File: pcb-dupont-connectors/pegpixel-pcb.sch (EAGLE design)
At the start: 6 parts

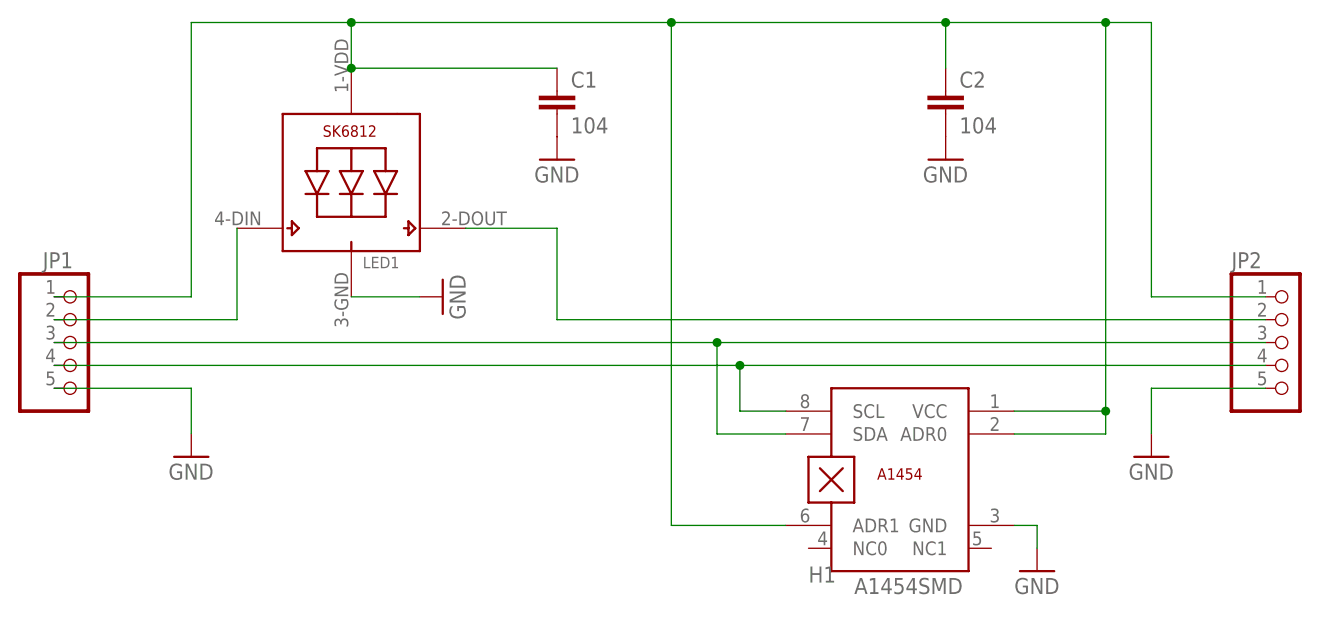
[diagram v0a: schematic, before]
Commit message: Remove second capacitor
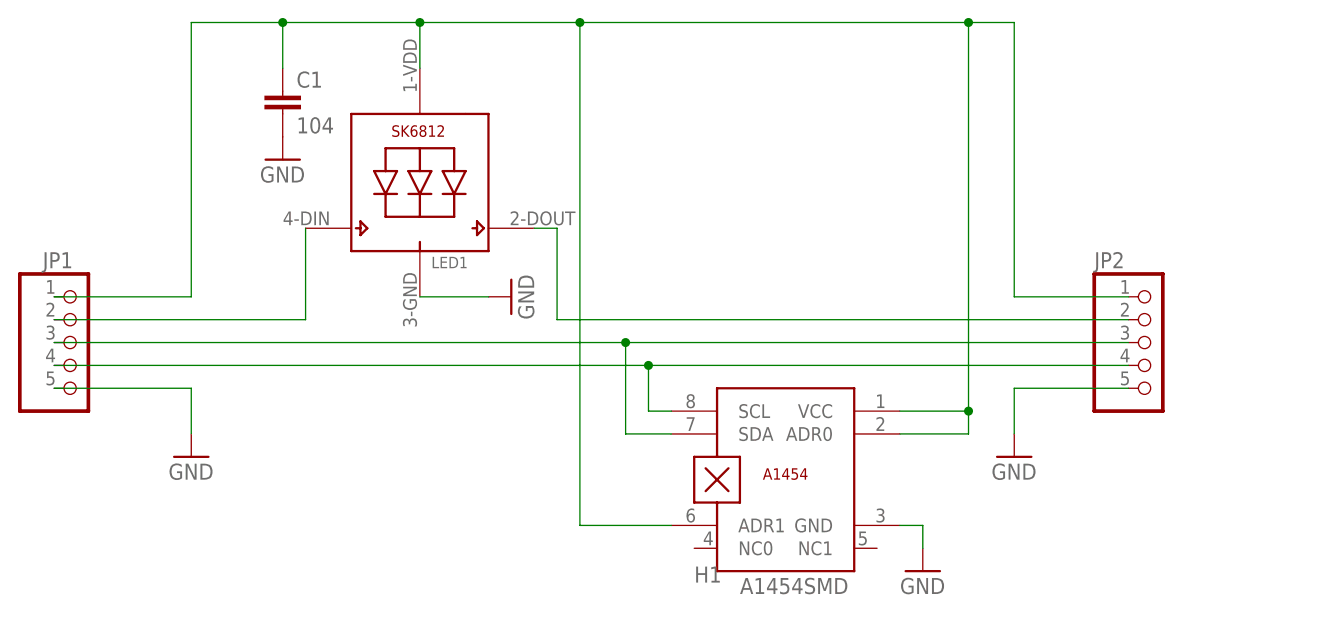
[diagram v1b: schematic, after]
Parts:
- removed C2: 104, rcl:C-EUC0805
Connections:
- net GND: no longer C2.2
- net VCC: no longer C2.1
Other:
- moved on the sheet: C1, H1, JP2, LED1

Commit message: pcb-design: add missing GRND-via
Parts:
- renumbered C1 to 104
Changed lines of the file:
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@@
 <parts>
 <part name="LED1" library="SK6812" deviceset="SK6812" device="_5050"/>
-<part name="C1" library="rcl" library_urn="urn:adsk.eagle:library:334" deviceset="C-EU" device="C0805" package3d_urn="urn:adsk.eagle:package:23617/2" value="104"/>
+<part name="104" library="rcl" library_urn="urn:adsk.eagle:library:334" deviceset="C-EU" device="C0805" package3d_urn="urn:adsk.eagle:package:23617/2" value="104"/>
 <part name="H1" library="a1454" deviceset="A1454" device="SMD" package3d_urn="urn:adsk.eagle:package:20813/2"/>
 <part name="GND1" library="supply1" library_urn="urn:adsk.eagle:library:371" deviceset="GND" device=""/>
@@
 <attribute name="VALUE" x="44.45" y="54.61" size="1.27" layer="96"/>
 </instance>
-<instance part="C1" gate="G$1" x="27.94" y="76.2" smashed="yes">
+<instance part="104" gate="G$1" x="27.94" y="76.2" smashed="yes">
 <attribute name="NAME" x="29.464" y="76.581" size="1.778" layer="95"/>
 <attribute name="VALUE" x="29.464" y="71.501" size="1.778" layer="96"/>
@@
 <junction x="104.14" y="83.82"/>
 <junction x="27.94" y="83.82"/>
-<pinref part="C1" gate="G$1" pin="1"/>
+<pinref part="104" gate="G$1" pin="1"/>
 <wire x1="27.94" y1="78.74" x2="27.94" y2="83.82" width="0.1524" layer="91"/>
 </segment>
@@
 <net name="GND" class="0">
 <segment>
-<pinref part="C1" gate="G$1" pin="2"/>
+<pinref part="104" gate="G$1" pin="2"/>
 <pinref part="GND3" gate="1" pin="GND"/>
 </segment>

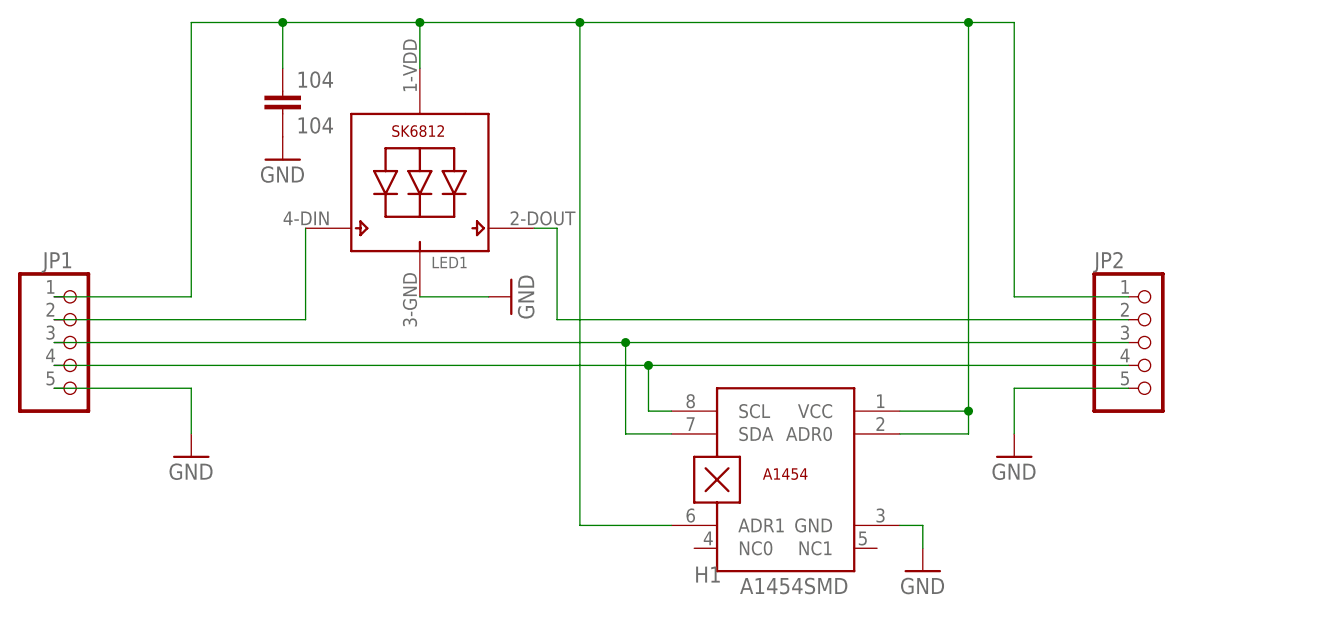
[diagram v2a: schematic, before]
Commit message: mirror and turn input pin header to place it on top layer
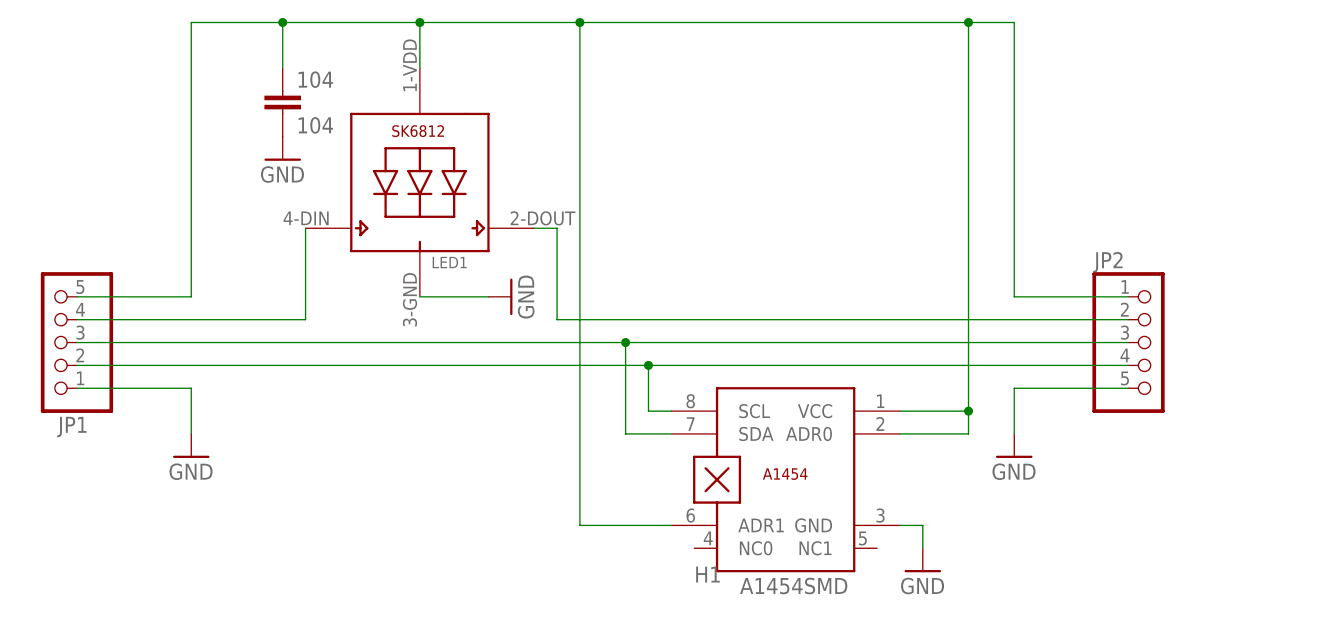
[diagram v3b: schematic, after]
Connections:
- net DIN: now also JP1.4; no longer JP1.2
- net GND: now also JP1.1; no longer JP1.5
- net SCL: now also JP1.2; no longer JP1.4
- net VCC: now also JP1.5; no longer JP1.1
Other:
- moved on the sheet: JP1
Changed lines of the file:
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@@
 <setting verticaltext="up"/>
 </settings>
-<grid distance="0.1" unitdist="inch" unit="inch" style="lines" multiple="1" display="yes" altdistance="0.01" altunitdist="inch" altunit="inch"/>
+<grid distance="0.1" unitdist="inch" unit="inch" style="lines" multiple="1" display="no" altdistance="0.01" altunitdist="inch" altunit="inch"/>
 <layers>
 <layer number="1" name="Top" color="4" fill="1" visible="no" active="no"/>
@@
 <attribute name="VALUE" x="55.88" y="50.8" size="1.778" layer="96" rot="R90"/>
 </instance>
-<instance part="JP1" gate="A" x="5.08" y="48.26" smashed="yes">
-<attribute name="NAME" x="1.27" y="56.515" size="1.778" layer="95"/>
-<attribute name="VALUE" x="-1.27" y="38.1" size="1.778" layer="96"/>
+<instance part="JP1" gate="A" x="2.54" y="48.26" smashed="yes" rot="R180">
+<attribute name="NAME" x="6.35" y="40.005" size="1.778" layer="95" rot="R180"/>
+<attribute name="VALUE" x="8.89" y="58.42" size="1.778" layer="96" rot="R180"/>
 </instance>
 <instance part="JP2" gate="A" x="124.46" y="48.26" smashed="yes">
@@
 <pinref part="LED1" gate="G$1" pin="VDD"/>
 <wire x1="43.18" y1="83.82" x2="43.18" y2="78.74" width="0.1524" layer="91"/>
-<pinref part="JP1" gate="A" pin="1"/>
-<wire x1="2.54" y1="53.34" x2="17.78" y2="53.34" width="0.1524" layer="91"/>
 <wire x1="17.78" y1="53.34" x2="17.78" y2="83.82" width="0.1524" layer="91"/>
 <wire x1="17.78" y1="83.82" x2="27.94" y2="83.82" width="0.1524" layer="91"/>
@@
 <pinref part="104" gate="G$1" pin="1"/>
 <wire x1="27.94" y1="78.74" x2="27.94" y2="83.82" width="0.1524" layer="91"/>
+<pinref part="JP1" gate="A" pin="5"/>
+<wire x1="5.08" y1="53.34" x2="17.78" y2="53.34" width="0.1524" layer="91"/>
 </segment>
 </net>
@@
 <pinref part="H1" gate="G$1" pin="SCL"/>
 <wire x1="68.58" y1="40.64" x2="71.12" y2="40.64" width="0.1524" layer="91"/>
-<pinref part="JP1" gate="A" pin="4"/>
 <pinref part="JP2" gate="A" pin="4"/>
-<wire x1="2.54" y1="45.72" x2="68.58" y2="45.72" width="0.1524" layer="91"/>
 <wire x1="68.58" y1="45.72" x2="121.92" y2="45.72" width="0.1524" layer="91"/>
 <wire x1="68.58" y1="40.64" x2="68.58" y2="45.72" width="0.1524" layer="91"/>
+<pinref part="JP1" gate="A" pin="2"/>
+<wire x1="5.08" y1="45.72" x2="68.58" y2="45.72" width="0.1524" layer="91"/>
 <junction x="68.58" y="45.72"/>
 </segment>
@@
 <wire x1="66.04" y1="38.1" x2="71.12" y2="38.1" width="0.1524" layer="91"/>
 <pinref part="JP1" gate="A" pin="3"/>
-<wire x1="2.54" y1="48.26" x2="66.04" y2="48.26" width="0.1524" layer="91"/>
+<wire x1="5.08" y1="48.26" x2="66.04" y2="48.26" width="0.1524" layer="91"/>
 <pinref part="JP2" gate="A" pin="3"/>
 <wire x1="66.04" y1="48.26" x2="121.92" y2="48.26" width="0.1524" layer="91"/>
@@
 </segment>
 <segment>
-<pinref part="JP1" gate="A" pin="5"/>
-<wire x1="2.54" y1="43.18" x2="17.78" y2="43.18" width="0.1524" layer="91"/>
 <pinref part="GND1" gate="1" pin="GND"/>
 <wire x1="17.78" y1="43.18" x2="17.78" y2="38.1" width="0.1524" layer="91"/>
+<pinref part="JP1" gate="A" pin="1"/>
+<wire x1="5.08" y1="43.18" x2="17.78" y2="43.18" width="0.1524" layer="91"/>
 </segment>
 <segment>
@@
 <net name="DIN" class="0">
 <segment>
-<pinref part="JP1" gate="A" pin="2"/>
 <pinref part="LED1" gate="G$1" pin="DI"/>
-<wire x1="2.54" y1="50.8" x2="30.48" y2="50.8" width="0.1524" layer="91"/>
 <wire x1="30.48" y1="50.8" x2="30.48" y2="60.96" width="0.1524" layer="91"/>
-</segment>
-</net>
+<pinref part="JP1" gate="A" pin="4"/>
+<wire x1="5.08" y1="50.8" x2="30.48" y2="50.8" width="0.1524" layer="91"/>
+</segment>
+</net>
